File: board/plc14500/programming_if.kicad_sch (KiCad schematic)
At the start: 6 parts, among them U3 74HC14, U6 Arduino Nano

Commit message: Address ERC errors
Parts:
- D17: footprint plc14500:LED_3MM -> LED_5MM; symbol plc14500-rescue:LED5MM-SparkFun-LED -> plc14500:LED
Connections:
- net WEN renamed !WEN
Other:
- note added: "The programmer asserts the PRG line to take control of the bus. This causes the PC address lines to go to HiZ. !WEN is cleared by the programmer once each program byte value and address is stable. This triggers a write in RAM. The programmer, or the user, can assert the RST line to cause a reset of the PC and of the lataches."
- note removed: "The programmer asserts the PRG line to take control of the bus. This causes the PC address lines to go to HiZ. WEN is asserted by the programmer once each program byte value and address is stable. This triggers a write in RAM. The programmer, or the user, can assert the RST line to cause a reset of the PC and of the lataches."
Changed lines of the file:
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@@
     (stroke (width 0) (type default))
   )
-  (text "The programmer asserts the PRG line to take control of the bus. This causes the PC address lines to go to HiZ.\n\nWEN is asserted by the programmer once each program byte value and address is stable. This triggers a write in RAM.\n\nThe programmer, or the user, can assert the RST line to cause a reset of the PC and of the lataches."
+  (text "The programmer asserts the PRG line to take control of the bus. This causes the PC address lines to go to HiZ.\n\n!WEN is cleared by the programmer once each program byte value and address is stable. This triggers a write in RAM.\n\nThe programmer, or the user, can assert the RST line to cause a reset of the PC and of the lataches."
     (at 123.825 54.61 0)
     (effects (font (size 1.27 1.27)) (justify left bottom))
@@
     (effects (font (size 1.27 1.27)) (justify left))
   )
-  (hierarchical_label "WEN" (shape output) (at 119.38 100.965 0) (fields_autoplaced)
+  (hierarchical_label "!WEN" (shape output) (at 119.38 100.965 0) (fields_autoplaced)
     (effects (font (size 1.27 1.27)) (justify left))
   )
@@
     )
   )
-  (symbol (lib_id "plc14500-rescue:LED5MM-SparkFun-LED") (at 156.21 107.315 0) (unit 1)
+  (symbol (lib_id "plc14500:LED") (at 156.21 107.315 0) (unit 1)
     (in_bom yes) (on_board yes) (dnp no)
     (property "Reference" "D17" (at 156.845 105.41 0)
@@
       (effects (font (size 1.143 1.143)) (justify left) hide)
     )
-    (property "Footprint" "plc14500:LED_3MM" (at 151.13 107.315 90)
+    (property "Footprint" "LED_5MM" (at 151.13 107.315 90)
       (effects (font (size 0.508 0.508)) hide)
     )
@@
       (effects (font (size 1.27 1.27)) hide)
     )
-    (property "Field4" "XXX-00000" (at 158.1912 110.7186 0)
-      (effects (font (size 1.524 1.524)) (justify left) hide)
+    (property "Field4" "XXX-00000" (at 149.86 107.315 90)
+      (effects (font (size 1.524 1.524)))
     )
     (property "Price" "0.01" (at 156.21 107.315 0)

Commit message: Cleanup, ready to route
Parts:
- D17: footprint LED_5MM -> plc14500:LED_3MM; Field4 XXX-00000 -> (none)
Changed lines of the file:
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@@
       (effects (font (size 1.143 1.143)) (justify left) hide)
     )
-    (property "Footprint" "LED_5MM" (at 151.13 107.315 90)
+    (property "Footprint" "plc14500:LED_3MM" (at 151.13 107.315 90)
       (effects (font (size 0.508 0.508)) hide)
     )
@@
       (effects (font (size 1.27 1.27)) hide)
     )
-    (property "Field4" "XXX-00000" (at 149.86 107.315 90)
+    (property "Field4" "" (at 149.86 107.315 90)
       (effects (font (size 1.524 1.524)))
     )

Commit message: Fix issues on REV.D0
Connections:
- net !RST renamed !RES
- net RST renamed RES
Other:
- note added: "The programmer asserts the PRG line to take control of the bus. This causes the PC address lines to go to HiZ. !WEN is cleared by the programmer once each program byte value and address is stable. This triggers a write in RAM. The programmer, or the user, can assert the RES line to cause a reset of the PC and of the lataches."
- note removed: "The programmer asserts the PRG line to take control of the bus. This causes the PC address lines to go to HiZ. !WEN is cleared by the programmer once each program byte value and address is stable. This triggers a write in RAM. The programmer, or the user, can assert the RST line to cause a reset of the PC and of the lataches."
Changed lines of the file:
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@@
     (stroke (width 0) (type default))
   )
-  (text "The programmer asserts the PRG line to take control of the bus. This causes the PC address lines to go to HiZ.\n\n!WEN is cleared by the programmer once each program byte value and address is stable. This triggers a write in RAM.\n\nThe programmer, or the user, can assert the RST line to cause a reset of the PC and of the lataches."
+  (text "The programmer asserts the PRG line to take control of the bus. This causes the PC address lines to go to HiZ.\n\n!WEN is cleared by the programmer once each program byte value and address is stable. This triggers a write in RAM.\n\nThe programmer, or the user, can assert the RES line to cause a reset of the PC and of the lataches."
     (at 123.825 54.61 0)
     (effects (font (size 1.27 1.27)) (justify left bottom))
@@
     (effects (font (size 1.27 1.27)) (justify right))
   )
-  (hierarchical_label "!RST" (shape output) (at 175.26 84.455 0) (fields_autoplaced)
+  (hierarchical_label "!RES" (shape output) (at 175.26 84.455 0) (fields_autoplaced)
     (effects (font (size 1.27 1.27)) (justify left))
   )
@@
     (effects (font (size 1.27 1.27)) (justify left))
   )
-  (hierarchical_label "RST" (shape bidirectional) (at 174.625 103.505 0) (fields_autoplaced)
+  (hierarchical_label "RES" (shape bidirectional) (at 174.625 103.505 0) (fields_autoplaced)
     (effects (font (size 1.27 1.27)) (justify left))
   )

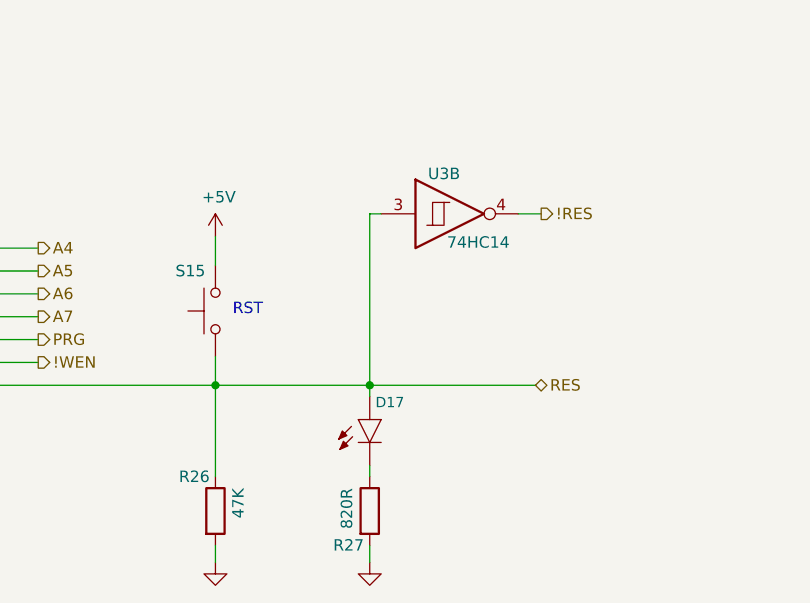
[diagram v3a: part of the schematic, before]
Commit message: Added reset cap from program line
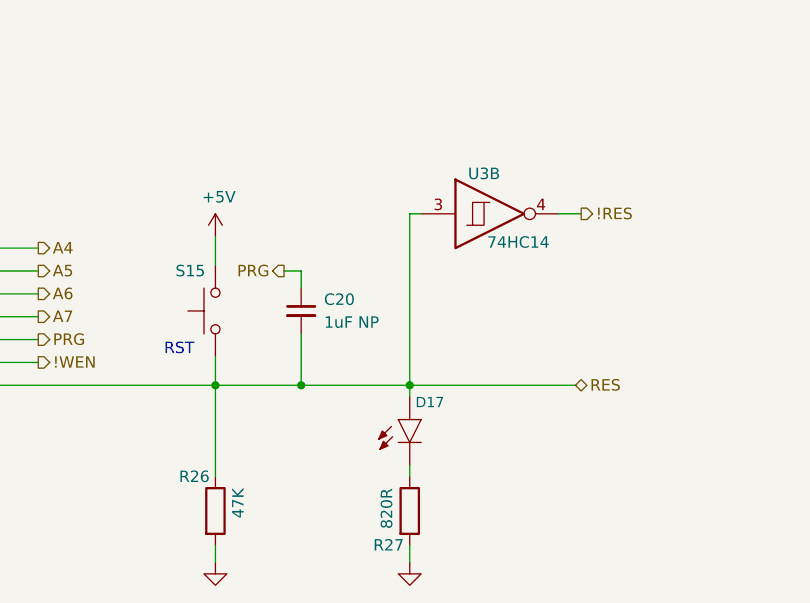
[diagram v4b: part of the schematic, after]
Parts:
- added C20: 1uF NP, Capacitor_THT:C_Radial_D6.3mm_H5.0mm_P2.50mm, symbol Device:C_Small
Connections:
- net PRG: now also C20.1
- net RES: now also C20.2
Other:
- moved on the sheet: D17, R27, U3B
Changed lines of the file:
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@@
     (comment 1 "REV.D")
   )
-  (junction (at 156.21 103.505) (diameter 0) (color 0 0 0 0)
+  (junction (at 148.59 103.505) (diameter 0) (color 0 0 0 0)
+  )
+  (junction (at 160.655 103.505) (diameter 0) (color 0 0 0 0)
   )
   (junction (at 97.79 113.665) (diameter 0) (color 0 0 0 0)
@@
     (stroke (width 0) (type default))
   )
-  (wire (pts (xy 156.21 103.505) (xy 156.21 104.775))
+  (wire (pts (xy 160.655 103.505) (xy 160.655 104.775))
     (stroke (width 0) (type default))
   )
@@
     (stroke (width 0) (type default))
   )
-  (wire (pts (xy 156.21 113.665) (xy 156.21 112.395))
+  (wire (pts (xy 160.655 113.665) (xy 160.655 112.395))
     (stroke (width 0) (type default))
   )
@@
     (stroke (width 0) (type default))
   )
-  (wire (pts (xy 139.065 103.505) (xy 156.21 103.505))
-    (stroke (width 0) (type default))
-  )
-  (wire (pts (xy 156.21 84.455) (xy 157.48 84.455))
-    (stroke (width 0) (type default))
-  )
-  (wire (pts (xy 156.21 103.505) (xy 156.21 84.455))
+  (wire (pts (xy 148.59 90.805) (xy 148.59 92.71))
+    (stroke (width 0) (type default))
+  )
+  (wire (pts (xy 139.065 103.505) (xy 148.59 103.505))
+    (stroke (width 0) (type default))
+  )
+  (wire (pts (xy 160.655 84.455) (xy 161.925 84.455))
+    (stroke (width 0) (type default))
+  )
+  (wire (pts (xy 160.655 103.505) (xy 160.655 84.455))
     (stroke (width 0) (type default))
   )
@@
     (stroke (width 0) (type default))
   )
+  (wire (pts (xy 148.59 103.505) (xy 160.655 103.505))
+    (stroke (width 0) (type default))
+  )
   (wire (pts (xy 83.82 88.265) (xy 78.74 88.265))
     (stroke (width 0) (type default))
   )
+  (wire (pts (xy 146.685 90.805) (xy 148.59 90.805))
+    (stroke (width 0) (type default))
+  )
   (wire (pts (xy 83.82 90.805) (xy 78.74 90.805))
     (stroke (width 0) (type default))
   )
-  (wire (pts (xy 156.21 121.285) (xy 156.21 123.19))
+  (wire (pts (xy 160.655 121.285) (xy 160.655 123.19))
     (stroke (width 0) (type default))
   )
@@
     (stroke (width 0) (type default))
   )
-  (wire (pts (xy 172.72 84.455) (xy 175.26 84.455))
+  (wire (pts (xy 177.165 84.455) (xy 179.705 84.455))
     (stroke (width 0) (type default))
   )
@@
     (stroke (width 0) (type default))
   )
+  (wire (pts (xy 148.59 97.79) (xy 148.59 103.505))
+    (stroke (width 0) (type default))
+  )
   (wire (pts (xy 97.79 113.665) (xy 99.06 113.665))
     (stroke (width 0) (type default))
   )
-  (wire (pts (xy 156.21 103.505) (xy 174.625 103.505))
+  (wire (pts (xy 160.655 103.505) (xy 179.07 103.505))
     (stroke (width 0) (type default))
   )
@@
     (effects (font (size 1.27 1.27)) (justify left bottom))
   )
-  (text "RST" (at 140.97 95.885 0)
+  (text "RST" (at 133.35 100.33 0)
     (effects (font (size 1.27 1.27)) (justify left bottom))
   )
@@
     (effects (font (size 1.27 1.27)) (justify left))
   )
+  (hierarchical_label "PRG" (shape output) (at 146.685 90.805 180) (fields_autoplaced)
+    (effects (font (size 1.27 1.27)) (justify right))
+  )
   (hierarchical_label "!WEN" (shape output) (at 119.38 100.965 0) (fields_autoplaced)
     (effects (font (size 1.27 1.27)) (justify left))
@@
     (effects (font (size 1.27 1.27)) (justify right))
   )
-  (hierarchical_label "!RES" (shape output) (at 175.26 84.455 0) (fields_autoplaced)
+  (hierarchical_label "!RES" (shape output) (at 179.705 84.455 0) (fields_autoplaced)
     (effects (font (size 1.27 1.27)) (justify left))
   )
@@
     (effects (font (size 1.27 1.27)) (justify left))
   )
-  (hierarchical_label "RES" (shape bidirectional) (at 174.625 103.505 0) (fields_autoplaced)
+  (hierarchical_label "RES" (shape bidirectional) (at 179.07 103.505 0) (fields_autoplaced)
     (effects (font (size 1.27 1.27)) (justify left))
   )
@@
     )
   )
-  (symbol (lib_id "power:GND") (at 156.21 123.19 0) (unit 1)
-    (in_bom yes) (on_board yes) (dnp no)
-    (property "Reference" "#PWR037" (at 156.21 129.54 0)
-      (effects (font (size 1.27 1.27)) hide)
-    )
-    (property "Value" "GND" (at 160.02 125.095 0)
-      (effects (font (size 1.27 1.27)) hide)
-    )
-    (property "Footprint" "" (at 156.21 123.19 0)
-      (effects (font (size 1.27 1.27)) hide)
-    )
-    (property "Datasheet" "" (at 156.21 123.19 0)
+  (symbol (lib_id "power:GND") (at 160.655 123.19 0) (unit 1)
+    (in_bom yes) (on_board yes) (dnp no)
+    (property "Reference" "#PWR037" (at 160.655 129.54 0)
+      (effects (font (size 1.27 1.27)) hide)
+    )
+    (property "Value" "GND" (at 164.465 125.095 0)
+      (effects (font (size 1.27 1.27)) hide)
+    )
+    (property "Footprint" "" (at 160.655 123.19 0)
+      (effects (font (size 1.27 1.27)) hide)
+    )
+    (property "Datasheet" "" (at 160.655 123.19 0)
       (effects (font (size 1.27 1.27)) hide)
     )
@@
     )
   )
-  (symbol (lib_id "plc14500:74HC14") (at 165.1 84.455 0) (unit 2)
-    (in_bom yes) (on_board yes) (dnp no)
-    (property "Reference" "U3" (at 164.465 80.01 0)
+  (symbol (lib_id "Device:C_Small") (at 148.59 95.25 0) (unit 1)
+    (in_bom yes) (on_board yes) (dnp no) (fields_autoplaced)
+    (property "Reference" "C20" (at 151.13 93.9863 0)
+      (effects (font (size 1.27 1.27)) (justify left))
+    )
+    (property "Value" "1uF NP" (at 151.13 96.5263 0)
+      (effects (font (size 1.27 1.27)) (justify left))
+    )
+    (property "Footprint" "Capacitor_THT:C_Radial_D6.3mm_H5.0mm_P2.50mm" (at 148.59 95.25 0)
+      (effects (font (size 1.27 1.27)) hide)
+    )
+    (property "Datasheet" "~" (at 148.59 95.25 0)
+      (effects (font (size 1.27 1.27)) hide)
+    )
+    (pin "1")
+    (pin "2")
+    (instances
+      (project "plc14500"
+        (path "/e5c24396-229a-4727-a88d-8f28d7f70179/8308f4d3-970f-416c-a310-08d544e11abe"
+          (reference "C20") (unit 1)
+        )
+      )
+    )
+  )
+  (symbol (lib_id "plc14500:74HC14") (at 169.545 84.455 0) (unit 2)
+    (in_bom yes) (on_board yes) (dnp no)
+    (property "Reference" "U3" (at 168.91 80.01 0)
       (effects (font (size 1.27 1.27)))
     )
-    (property "Value" "74HC14" (at 168.275 87.63 0)
+    (property "Value" "74HC14" (at 172.72 87.63 0)
       (effects (font (size 1.27 1.27)))
     )
-    (property "Footprint" "Package_DIP:DIP-14_W7.62mm_LongPads" (at 165.1 84.455 0)
-      (effects (font (size 1.27 1.27)) hide)
-    )
-    (property "Datasheet" "http://www.ti.com/lit/gpn/sn74HC14" (at 165.1 84.455 0)
-      (effects (font (size 1.27 1.27)) hide)
-    )
-    (property "Price" "0.16" (at 165.1 84.455 0)
+    (property "Footprint" "Package_DIP:DIP-14_W7.62mm_LongPads" (at 169.545 84.455 0)
+      (effects (font (size 1.27 1.27)) hide)
+    )
+    (property "Datasheet" "http://www.ti.com/lit/gpn/sn74HC14" (at 169.545 84.455 0)
+      (effects (font (size 1.27 1.27)) hide)
+    )
+    (property "Price" "0.16" (at 169.545 84.455 0)
       (effects (font (size 1.27 1.27)) hide)
     )
@@
     )
   )
-  (symbol (lib_id "Device:R") (at 156.21 117.475 0) (unit 1)
-    (in_bom yes) (on_board yes) (dnp no)
-    (property "Reference" "R27" (at 155.575 121.285 0)
+  (symbol (lib_id "Device:R") (at 160.655 117.475 0) (unit 1)
+    (in_bom yes) (on_board yes) (dnp no)
+    (property "Reference" "R27" (at 160.02 121.285 0)
       (effects (font (size 1.27 1.27)) (justify right))
     )
-    (property "Value" "820R" (at 153.67 114.935 90)
+    (property "Value" "820R" (at 158.115 114.935 90)
       (effects (font (size 1.27 1.27)) (justify right))
     )
-    (property "Footprint" "Resistor_THT:R_Axial_DIN0204_L3.6mm_D1.6mm_P7.62mm_Horizontal" (at 154.432 117.475 90)
-      (effects (font (size 1.27 1.27)) hide)
-    )
-    (property "Datasheet" "~" (at 156.21 117.475 0)
-      (effects (font (size 1.27 1.27)) hide)
-    )
-    (property "Price" "0.01" (at 156.21 117.475 0)
+    (property "Footprint" "Resistor_THT:R_Axial_DIN0204_L3.6mm_D1.6mm_P7.62mm_Horizontal" (at 158.877 117.475 90)
+      (effects (font (size 1.27 1.27)) hide)
+    )
+    (property "Datasheet" "~" (at 160.655 117.475 0)
+      (effects (font (size 1.27 1.27)) hide)
+    )
+    (property "Price" "0.01" (at 160.655 117.475 0)
       (effects (font (size 1.27 1.27)) hide)
     )
@@
     )
   )
-  (symbol (lib_id "plc14500:LED") (at 156.21 107.315 0) (unit 1)
-    (in_bom yes) (on_board yes) (dnp no)
-    (property "Reference" "D17" (at 156.845 105.41 0)
+  (symbol (lib_id "plc14500:LED") (at 160.655 107.315 0) (unit 1)
+    (in_bom yes) (on_board yes) (dnp no)
+    (property "Reference" "D17" (at 161.29 105.41 0)
       (effects (font (size 1.143 1.143)) (justify left))
     )
-    (property "Value" "LED 3MM Red" (at 158.1912 108.3056 0)
+    (property "Value" "LED 3MM Red" (at 162.6362 108.3056 0)
       (effects (font (size 1.143 1.143)) (justify left) hide)
     )
-    (property "Footprint" "plc14500:LED_3MM" (at 151.13 107.315 90)
+    (property "Footprint" "plc14500:LED_3MM" (at 155.575 107.315 90)
       (effects (font (size 0.508 0.508)) hide)
     )
-    (property "Datasheet" "" (at 156.21 107.315 0)
-      (effects (font (size 1.27 1.27)) hide)
-    )
-    (property "Field4" "" (at 149.86 107.315 90)
+    (property "Datasheet" "" (at 160.655 107.315 0)
+      (effects (font (size 1.27 1.27)) hide)
+    )
+    (property "Field4" "" (at 154.305 107.315 90)
       (effects (font (size 1.524 1.524)))
     )
-    (property "Price" "0.01" (at 156.21 107.315 0)
-      (effects (font (size 1.27 1.27)) hide)
-    )
+    (property "Price" "0.01" (at 160.655 107.315 0)
+      (effects (font (size 1.27 1.27)) hide)
+    )
